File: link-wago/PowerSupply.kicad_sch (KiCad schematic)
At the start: 8 parts, among them U501 TPSM33625

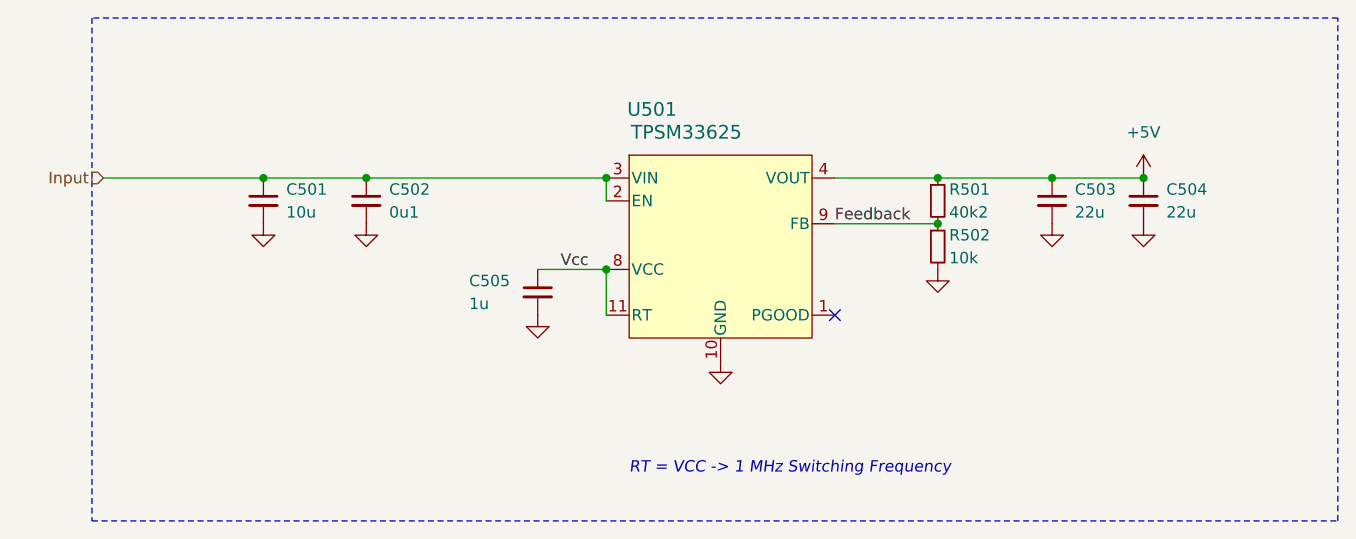
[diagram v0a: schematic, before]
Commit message: Update power symbols
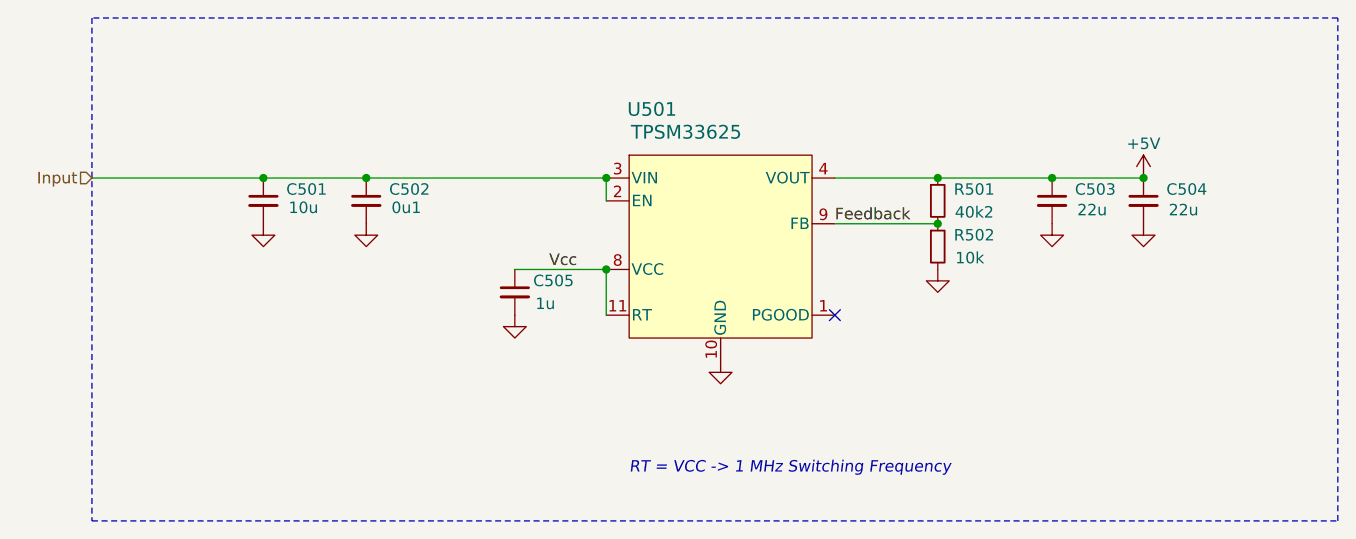
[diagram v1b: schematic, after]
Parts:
- C501: footprint Capacitor_SMD:C_1210_3225Metric -> V2_Capacitor_SMD:C_1210; symbol Device:C_Small -> V2_Device:C_1210_10u; Mouser (none) -> 810-CNA6P1X7R1H106K2; Rating (none) -> 50V
- C502: footprint Capacitor_SMD:C_0603_1608Metric -> V2_Capacitor_SMD:C_0603; symbol Device:C_Small -> V2_Device:C_0603_0u1; Mouser (none) -> 810-CGA3E2X7R1H104MA
- C503, C504: footprint Capacitor_SMD:C_1210_3225Metric -> V2_Capacitor_SMD:C_1210; symbol Device:C_Small -> V2_Device:C_1210_22u; Mouser (none) -> 810-CGA6P3X7R1E226M5; Rating (none) -> 25V
- C505: footprint Capacitor_SMD:C_0603_1608Metric -> V2_Capacitor_SMD:C_0603; symbol Device:C_Small -> V2_Device:C_0603_1u; Mouser (none) -> 810-CGA3E2X7R1H104MA
- R501: footprint Resistor_SMD:R_0603_1608Metric -> V2_Resistor_SMD:R_0603; symbol Device:R_Small -> V2_Device:R_0603_40k2; Mouser (none) -> 71-RCS060340K2FKEA
- R502: footprint Resistor_SMD:R_0603_1608Metric -> V2_Resistor_SMD:R_0603; symbol Device:R_Small -> V2_Device:R_0603_10k; Mouser (none) -> 71-CRCW060310K0FKEAC
- U501: Mouser (none) -> 595-TPSM33625RDNR
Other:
- moved on the sheet: C505

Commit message: Refresh
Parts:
- C501: Manufacturer (none) -> TDK; Product (none) -> CNA6P1X7R1H106K250AE; Rating 50V -> (none); Voltage (none) -> 50V
- C502: Manufacturer (none) -> TDK; Product (none) -> CGA3E2X7R1H104M080AA
- C503, C504: Manufacturer (none) -> TDK; Product (none) -> CGA6P3X7R1E226M250AE; Rating 25V -> (none); Voltage (none) -> 25V
- C505: Manufacturer (none) -> YAGEO; Mouser 810-CGA3E2X7R1H104MA -> 603-CC603KRX7R9BB105; Product (none) -> CC0603KRX7R9BB105
- R501: Manufacturer (none) -> Vishay; Product (none) -> RCS060340K2FKEA; Rating (none) -> 500mW
- R502: Manufacturer (none) -> Vishay; Product (none) -> CRCW060310K0FKEAC; Rating (none) -> 100mW
- U501: Manufacturer (none) -> Texas Instruments; Product (none) -> TPSM33625RDNR
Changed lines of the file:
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@@
+			)
+		)
+		(property "Manufacturer" "Texas Instruments"
+			(at 148.59 146.05 0)
+			(effects
+				(font
+					(size 1.27 1.27)
+				)
+				(hide yes)
+			)
+		)
+		(property "Product" "TPSM33625RDNR"
+			(at 148.59 148.59 0)
+			(effects
+				(font
+					(size 1.27 1.27)
+				)
+				(hide yes)
 			)
 		)
@@
 			)
 		)
+		(property "Manufacturer" "TDK"
+			(at 109.22 113.03 0)
+			(effects
+				(font
+					(size 1.27 1.27)
+				)
+				(hide yes)
+			)
+		)
+		(property "Product" "CGA3E2X7R1H104M080AA"
+			(at 109.22 115.57 0)
+			(effects
+				(font
+					(size 1.27 1.27)
+				)
+				(hide yes)
+			)
+		)
 		(pin "1"
 		)
@@
 			)
 		)
-		(property "Rating" "25V"
-			(at 195.58 117.094 0)
+		(property "Voltage" "25V"
+			(at 195.58 118.11 0)
+			(effects
+				(font
+					(size 1.27 1.27)
+				)
+				(hide yes)
+			)
+		)
+		(property "Product" "CGA6P3X7R1E226M250AE"
+			(at 195.58 115.57 0)
+			(effects
+				(font
+					(size 1.27 1.27)
+				)
+				(hide yes)
+			)
+		)
+		(property "Manufacturer" "TDK"
+			(at 195.58 113.03 0)
 			(effects
 				(font
@@
 			)
 		)
+		(property "Rating" "500mW"
+			(at 172.72 118.11 0)
+			(effects
+				(font
+					(size 1.27 1.27)
+				)
+				(hide yes)
+			)
+		)
+		(property "Manufacturer" "Vishay"
+			(at 172.72 113.03 0)
+			(effects
+				(font
+					(size 1.27 1.27)
+				)
+				(hide yes)
+			)
+		)
+		(property "Product" "RCS060340K2FKEA"
+			(at 172.72 115.57 0)
+			(effects
+				(font
+					(size 1.27 1.27)
+				)
+				(hide yes)
+			)
+		)
 		(pin "1"
 		)
@@
 			)
 		)
-		(property "Mouser" "810-CGA3E2X7R1H104MA"
+		(property "Mouser" "603-CC603KRX7R9BB105"
 			(at 125.73 125.222 0)
+			(effects
+				(font
+					(size 1.27 1.27)
+				)
+				(hide yes)
+			)
+		)
+		(property "Product" "CC0603KRX7R9BB105"
+			(at 125.73 125.73 0)
+			(effects
+				(font
+					(size 1.27 1.27)
+				)
+				(hide yes)
+			)
+		)
+		(property "Manufacturer" "YAGEO"
+			(at 125.73 123.19 0)
 			(effects
 				(font
@@
 			)
 		)
-		(property "Rating" "25V"
-			(at 185.42 117.094 0)
+		(property "Voltage" "25V"
+			(at 185.42 118.11 0)
+			(effects
+				(font
+					(size 1.27 1.27)
+				)
+				(hide yes)
+			)
+		)
+		(property "Product" "CGA6P3X7R1E226M250AE"
+			(at 185.42 115.57 0)
+			(effects
+				(font
+					(size 1.27 1.27)
+				)
+				(hide yes)
+			)
+		)
+		(property "Manufacturer" "TDK"
+			(at 185.42 113.03 0)
 			(effects
 				(font
@@
 			)
 		)
+		(property "Product" "CRCW060310K0FKEAC"
+			(at 172.72 120.65 0)
+			(effects
+				(font
+					(size 1.27 1.27)
+				)
+				(hide yes)
+			)
+		)
+		(property "Manufacturer" "Vishay"
+			(at 172.72 118.11 0)
+			(effects
+				(font
+					(size 1.27 1.27)
+				)
+				(hide yes)
+			)
+		)
+		(property "Rating" "100mW"
+			(at 172.72 123.19 0)
+			(effects
+				(font
+					(size 1.27 1.27)
+				)
+				(hide yes)
+			)
+		)
 		(pin "1"
 		)
@@
 			)
 		)
-		(property "Rating" "50V"
-			(at 97.79 116.84 0)
-			(effects
-				(font
+		(property "Voltage" "50V"
+			(at 97.79 118.11 0)
+			(effects
+				(font
+					(size 1.27 1.27)
+				)
+				(hide yes)
+			)
+		)
+		(property "Product" "CNA6P1X7R1H106K250AE"
+			(at 97.79 115.57 0)
+			(effects
+				(font
+					(size 1.27 1.27)
+				)
+				(hide yes)
+			)
+		)
+		(property "Manufacturer" "TDK"
+			(at 97.79 113.03 0)
+			(effects
+				(font

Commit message: Fix WAGOs
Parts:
- C505: Rating (none) -> 50V
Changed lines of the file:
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@@
+			)
+		)
+		(property "Rating" "50V"
+			(at 125.73 130.81 0)
+			(effects
+				(font
+					(size 1.27 1.27)
+				)
+				(hide yes)
 			)
 		)

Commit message: Refresh
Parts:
- C501: Rating (none) -> 50V; Voltage 50V -> (none)
- C502: Rating (none) -> 50V
- C503, C504: Rating (none) -> 25V; Voltage 25V -> (none)
- C505: Manufacturer YAGEO -> TDK; Mouser 603-CC603KRX7R9BB105 -> 810-CGA3E3X7R1H105K0; Product CC0603KRX7R9BB105 -> CGA3E3X7R1H105K080AB
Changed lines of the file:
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@@
+			)
+		)
+		(property "Rating" "50V"
+			(at 109.22 120.65 0)
+			(effects
+				(font
+					(size 1.27 1.27)
+				)
+				(hide yes)
 			)
 		)
@@
 			)
 		)
-		(property "Voltage" "25V"
-			(at 195.58 118.11 0)
-			(effects
-				(font
-					(size 1.27 1.27)
-				)
-				(hide yes)
-			)
-		)
 		(property "Product" "CGA6P3X7R1E226M250AE"
 			(at 195.58 115.57 0)
@@
 			)
 		)
+		(property "Rating" "25V"
+			(at 195.58 118.11 0)
+			(effects
+				(font
+					(size 1.27 1.27)
+				)
+				(hide yes)
+			)
+		)
 		(pin "1"
 		)
@@
 			)
 		)
-		(property "Mouser" "603-CC603KRX7R9BB105"
+		(property "Mouser" "810-CGA3E3X7R1H105K0"
 			(at 125.73 125.222 0)
 			(effects
@@
 			)
 		)
-		(property "Product" "CC0603KRX7R9BB105"
+		(property "Product" "CGA3E3X7R1H105K080AB"
 			(at 125.73 125.73 0)
 			(effects
@@
 			)
 		)
-		(property "Manufacturer" "YAGEO"
+		(property "Manufacturer" "TDK"
 			(at 125.73 123.19 0)
 			(effects
@@
 			)
 		)
-		(property "Voltage" "25V"
-			(at 185.42 118.11 0)
-			(effects
-				(font
-					(size 1.27 1.27)
-				)
-				(hide yes)
-			)
-		)
 		(property "Product" "CGA6P3X7R1E226M250AE"
 			(at 185.42 115.57 0)
@@
 			)
 		)
+		(property "Rating" "25V"
+			(at 185.42 118.11 0)
+			(effects
+				(font
+					(size 1.27 1.27)
+				)
+				(hide yes)
+			)
+		)
 		(pin "1"
 		)
@@
 			)
 		)
-		(property "Voltage" "50V"
-			(at 97.79 118.11 0)
-			(effects
-				(font
-					(size 1.27 1.27)
-				)
-				(hide yes)
-			)
-		)
 		(property "Product" "CNA6P1X7R1H106K250AE"
 			(at 97.79 115.57 0)
@@
 			(effects
 				(font
+					(size 1.27 1.27)
+				)
+				(hide yes)
+			)
+		)
+		(property "Rating" "50V"
+			(at 97.79 118.11 0)
+			(effects
+				(font

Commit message: Update library
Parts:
- U501: footprint V2_Converter_DCDC:TPSM33625 -> V2_Converter_DCDC:QFN-11; symbol V2_Converter_DCDC:TPSM33625 -> V2_Converter_DCDC:TPSM33625RDNR; Rating (none) -> 2.5A
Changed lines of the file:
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@@
 	)
 	(symbol
-		(lib_id "V2_Converter_DCDC:TPSM33625")
+		(lib_id "V2_Converter_DCDC:TPSM33625RDNR")
 		(at 148.59 102.87 0)
 		(unit 1)
@@
 		)
 		(property "Value" "TPSM33625"
-			(at 144.78 90.17 0)
+			(at 138.176 90.17 0)
 			(effects
 				(font
 					(size 1.524 1.524)
 				)
+				(justify left)
 			)
 		)
-		(property "Footprint" "V2_Converter_DCDC:TPSM33625"
-			(at 148.59 118.11 0)
+		(property "Footprint" "V2_Converter_DCDC:QFN-11"
+			(at 148.59 140.97 0)
 			(effects
 				(font
@@
 			)
 		)
-		(property "Datasheet" "https://www.ti.com/lit/ds/symlink/tpsm33625.pdf"
-			(at 153.67 118.11 0)
+		(property "Datasheet" ""
+			(at 148.59 143.51 0)
 			(effects
 				(font
@@
 		)
 		(property "Mouser" "595-TPSM33625RDNR"
-			(at 148.59 102.87 0)
+			(at 148.59 151.13 0)
+			(show_name yes)
 			(effects
 				(font
@@
 		(property "Manufacturer" "Texas Instruments"
 			(at 148.59 146.05 0)
+			(show_name yes)
 			(effects
 				(font
@@
 		(property "Product" "TPSM33625RDNR"
 			(at 148.59 148.59 0)
+			(show_name yes)
 			(effects
 				(font
+					(size 1.27 1.27)
+				)
+				(hide yes)
+			)
+		)
+		(property "Rating" "2.5A"
+			(at 148.59 153.67 0)
+			(effects
+				(font

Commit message: Update Library
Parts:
- C501: symbol V2_Device:C_1210_10u -> V2_Capacitor:1210_10u
- C502: symbol V2_Device:C_0603_0u1 -> V2_Capacitor:0603_0u1
- C503, C504: symbol V2_Device:C_1210_22u -> V2_Capacitor:1210_22u
- C505: symbol V2_Device:C_0603_1u -> V2_Capacitor:0603_1u
- R501: symbol V2_Device:R_0603_40k2 -> V2_Resistor:0603_40k2
- R502: symbol V2_Device:R_0603_10k -> V2_Resistor:0603_10k
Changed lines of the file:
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@@
 	)
 	(symbol
-		(lib_id "V2_Device:C_0603_0u1")
+		(lib_id "V2_Capacitor:0603_0u1")
 		(at 109.22 97.79 0)
 		(unit 1)
@@
 	)
 	(symbol
-		(lib_id "V2_Device:C_1210_22u")
+		(lib_id "V2_Capacitor:1210_22u")
 		(at 195.58 97.79 0)
 		(unit 1)
@@
 	)
 	(symbol
-		(lib_id "V2_Device:R_0603_40k2")
+		(lib_id "V2_Resistor:0603_40k2")
 		(at 172.72 97.79 0)
 		(unit 1)
@@
 	)
 	(symbol
-		(lib_id "V2_Device:C_0603_1u")
+		(lib_id "V2_Capacitor:0603_1u")
 		(at 125.73 107.95 0)
 		(unit 1)
@@
 	)
 	(symbol
-		(lib_id "V2_Device:C_1210_22u")
+		(lib_id "V2_Capacitor:1210_22u")
 		(at 185.42 97.79 0)
 		(unit 1)
@@
 	)
 	(symbol
-		(lib_id "V2_Device:R_0603_10k")
+		(lib_id "V2_Resistor:0603_10k")
 		(at 172.72 102.87 0)
 		(unit 1)
@@
 	)
 	(symbol
-		(lib_id "V2_Device:C_1210_10u")
+		(lib_id "V2_Capacitor:1210_10u")
 		(at 97.79 97.79 0)
 		(unit 1)
